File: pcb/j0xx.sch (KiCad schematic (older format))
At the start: 73 parts

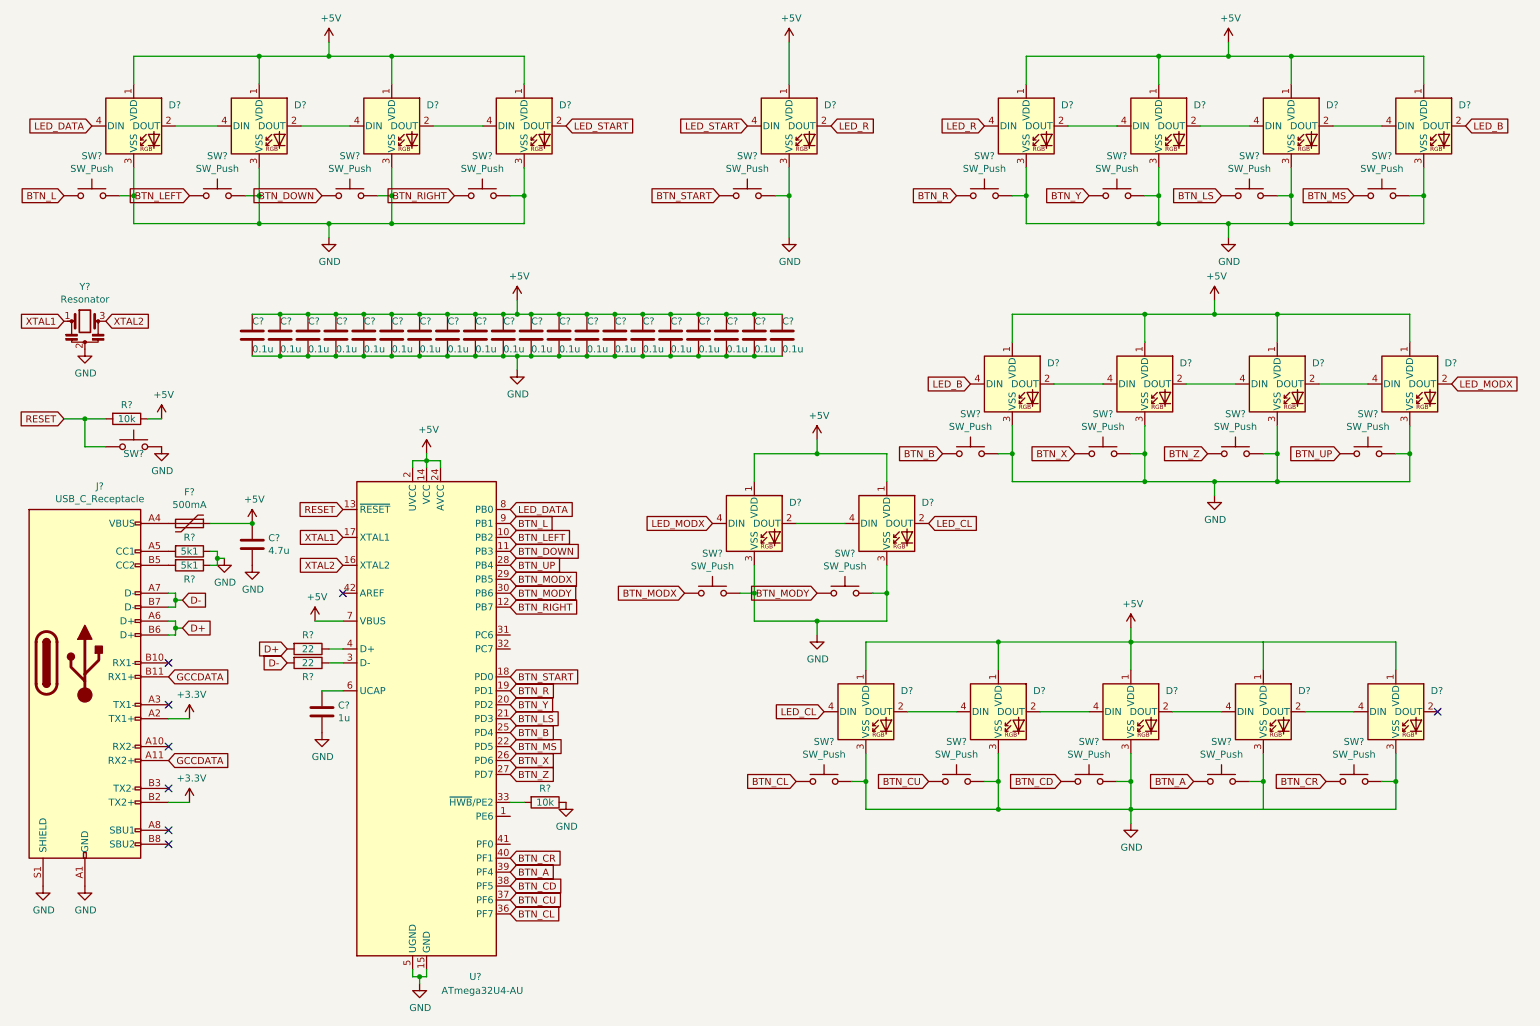
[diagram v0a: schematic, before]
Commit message: added footprints
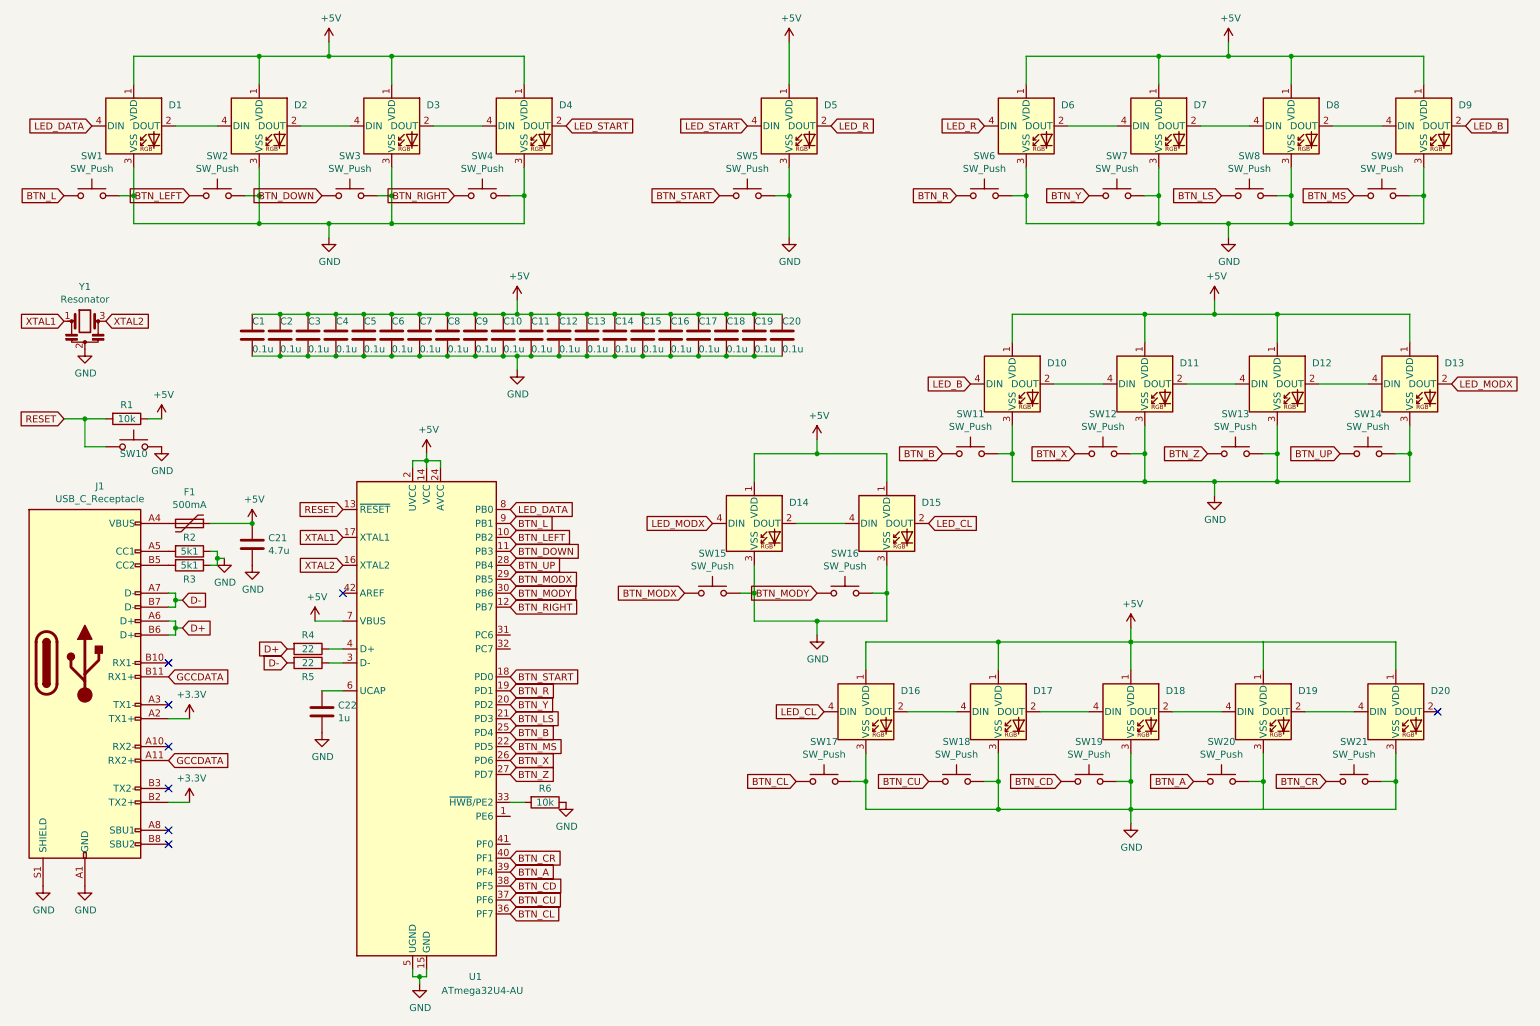
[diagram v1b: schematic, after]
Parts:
- C1, C10, C11, C12, C13, C14, C15, C16, C17, C18, C19, C2, C20, C21, C22, C3, C4, C5, C6, C7, C8, C9: renamed from C?; footprint (none) -> Capacitor_SMD:C_0805_2012Metric
- F1: renamed from F?; footprint (none) -> Fuse:Fuse_1206_3216Metric
- J1: renamed from J?; footprint (none) -> Connector_USB:USB_C_Receptacle_Amphenol_12401610E4-2A
- R1, R2, R3, R4, R5, R6: renamed from R?; footprint (none) -> Resistor_SMD:R_0805_2012Metric
- SW1, SW11, SW12, SW13, SW14, SW15, SW16, SW17, SW18, SW19, SW2, SW20, SW21, SW3, SW4, SW5, SW6, SW7, SW8, SW9: renamed from SW?; footprint (none) -> Button_Switch_Keyboard:SW_Cherry_MX_1.00u_PCB
- SW10: renamed from SW?; footprint (none) -> TestPoint:TestPoint_Bridge_Pitch3.81mm_Drill1.3mm
- Y1: renamed from Y?; footprint (none) -> Crystal:Resonator_SMD_muRata_CSTxExxV-3Pin_3.0x1.1mm
- gave numbers to parts that had none: 21

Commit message: Initial PCB work
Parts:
- SW0: renamed from SW10; footprint TestPoint:TestPoint_Bridge_Pitch3.81mm_Drill1.3mm -> TestPoint:TestPoint_2Pads_Pitch2.54mm_Drill0.8mm
- renumbered SW11 to SW10, SW12 to SW11, SW13 to SW12, SW14 to SW13, SW15 to SW14, SW16 to SW15, SW17 to SW16, SW18 to SW17, SW19 to SW18, SW20 to SW19, SW21 to SW20
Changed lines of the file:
@@
 	1100 3400 950  3400
 $Comp
-L Switch:SW_Push SW10
+L Switch:SW_Push SW0
 U 1 1 610B7F02
 P 1300 3600
-F 0 "SW10" H 1300 3550 50  0000 C CNN
+F 0 "SW0" H 1300 3507 50  0000 C CNN
 F 1 "reset" H 1300 3794 50  0001 C CNN
-F 2 "TestPoint:TestPoint_Bridge_Pitch3.81mm_Drill1.3mm" H 1300 3800 50  0001 C CNN
+F 2 "TestPoint:TestPoint_2Pads_Pitch2.54mm_Drill0.8mm" H 1300 3800 50  0001 C CNN
 F 3 "~" H 1300 3800 50  0001 C CNN
 	1    1300 3600
@@
 	9600 800  9150 800
 $Comp
-L Switch:SW_Push SW11
+L Switch:SW_Push SW10
 U 1 1 61154D84
 P 7300 3650
-F 0 "SW11" H 7300 3935 50  0000 C CNN
+F 0 "SW10" H 7300 3935 50  0000 C CNN
 F 1 "SW_Push" H 7300 3844 50  0000 C CNN
 F 2 "Button_Switch_Keyboard:SW_Cherry_MX_1.00u_PCB" H 7300 3850 50  0001 C CNN
@@
 	7500 3650 7600 3650
 $Comp
-L Switch:SW_Push SW12
+L Switch:SW_Push SW11
 U 1 1 61154D93
 P 8250 3650
-F 0 "SW12" H 8250 3935 50  0000 C CNN
+F 0 "SW11" H 8250 3935 50  0000 C CNN
 F 1 "SW_Push" H 8250 3844 50  0000 C CNN
 F 2 "Button_Switch_Keyboard:SW_Cherry_MX_1.00u_PCB" H 8250 3850 50  0001 C CNN
@@
 	8450 3650 8550 3650
 $Comp
-L Switch:SW_Push SW13
+L Switch:SW_Push SW12
 U 1 1 61154DA1
 P 9200 3650
-F 0 "SW13" H 9200 3935 50  0000 C CNN
+F 0 "SW12" H 9200 3935 50  0000 C CNN
 F 1 "SW_Push" H 9200 3844 50  0000 C CNN
 F 2 "Button_Switch_Keyboard:SW_Cherry_MX_1.00u_PCB" H 9200 3850 50  0001 C CNN
@@
 	7600 3850 8550 3850
 $Comp
-L Switch:SW_Push SW14
+L Switch:SW_Push SW13
 U 1 1 61154DBF
 P 10150 3650
-F 0 "SW14" H 10150 3935 50  0000 C CNN
+F 0 "SW13" H 10150 3935 50  0000 C CNN
 F 1 "SW_Push" H 10150 3844 50  0000 C CNN
 F 2 "Button_Switch_Keyboard:SW_Cherry_MX_1.00u_PCB" H 10150 3850 50  0001 C CNN
@@
 	9050 3850 9500 3850
 $Comp
-L Switch:SW_Push SW15
+L Switch:SW_Push SW14
 U 1 1 611ACA7D
 P 5450 4650
-F 0 "SW15" H 5450 4935 50  0000 C CNN
+F 0 "SW14" H 5450 4935 50  0000 C CNN
 F 1 "SW_Push" H 5450 4844 50  0000 C CNN
 F 2 "Button_Switch_Keyboard:SW_Cherry_MX_1.00u_PCB" H 5450 4850 50  0001 C CNN
@@
 	5650 4650 5750 4650
 $Comp
-L Switch:SW_Push SW16
+L Switch:SW_Push SW15
 U 1 1 611ACA8C
 P 6400 4650
-F 0 "SW16" H 6400 4935 50  0000 C CNN
+F 0 "SW15" H 6400 4935 50  0000 C CNN
 F 1 "SW_Push" H 6400 4844 50  0000 C CNN
 F 2 "Button_Switch_Keyboard:SW_Cherry_MX_1.00u_PCB" H 6400 4850 50  0001 C CNN
@@
 	6200 4850 6700 4850
 $Comp
-L Switch:SW_Push SW17
+L Switch:SW_Push SW16
 U 1 1 611CDB45
 P 6250 6000
-F 0 "SW17" H 6250 6285 50  0000 C CNN
+F 0 "SW16" H 6250 6285 50  0000 C CNN
 F 1 "SW_Push" H 6250 6194 50  0000 C CNN
 F 2 "Button_Switch_Keyboard:SW_Cherry_MX_1.00u_PCB" H 6250 6200 50  0001 C CNN
@@
 	6450 6000 6550 6000
 $Comp
-L Switch:SW_Push SW18
+L Switch:SW_Push SW17
 U 1 1 611CDB54
 P 7200 6000
-F 0 "SW18" H 7200 6285 50  0000 C CNN
+F 0 "SW17" H 7200 6285 50  0000 C CNN
 F 1 "SW_Push" H 7200 6194 50  0000 C CNN
 F 2 "Button_Switch_Keyboard:SW_Cherry_MX_1.00u_PCB" H 7200 6200 50  0001 C CNN
@@
 	7400 6000 7500 6000
 $Comp
-L Switch:SW_Push SW19
+L Switch:SW_Push SW18
 U 1 1 611CDB62
 P 8150 6000
-F 0 "SW19" H 8150 6285 50  0000 C CNN
+F 0 "SW18" H 8150 6285 50  0000 C CNN
 F 1 "SW_Push" H 8150 6194 50  0000 C CNN
 F 2 "Button_Switch_Keyboard:SW_Cherry_MX_1.00u_PCB" H 8150 6200 50  0001 C CNN
@@
 	6550 6200 7500 6200
 $Comp
-L Switch:SW_Push SW20
+L Switch:SW_Push SW19
 U 1 1 611CDB7D
 P 9100 6000
-F 0 "SW20" H 9100 6285 50  0000 C CNN
+F 0 "SW19" H 9100 6285 50  0000 C CNN
 F 1 "SW_Push" H 9100 6194 50  0000 C CNN
 F 2 "Button_Switch_Keyboard:SW_Cherry_MX_1.00u_PCB" H 9100 6200 50  0001 C CNN
@@
 LED_CL
 $Comp
-L Switch:SW_Push SW21
+L Switch:SW_Push SW20
 U 1 1 61200F3C
 P 10050 6000
-F 0 "SW21" H 10050 6285 50  0000 C CNN
+F 0 "SW20" H 10050 6285 50  0000 C CNN
 F 1 "SW_Push" H 10050 6194 50  0000 C CNN
 F 2 "Button_Switch_Keyboard:SW_Cherry_MX_1.00u_PCB" H 10050 6200 50  0001 C CNN
